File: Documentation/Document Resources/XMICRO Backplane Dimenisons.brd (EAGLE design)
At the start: 203.2 x 70.6 mm, 5 parts

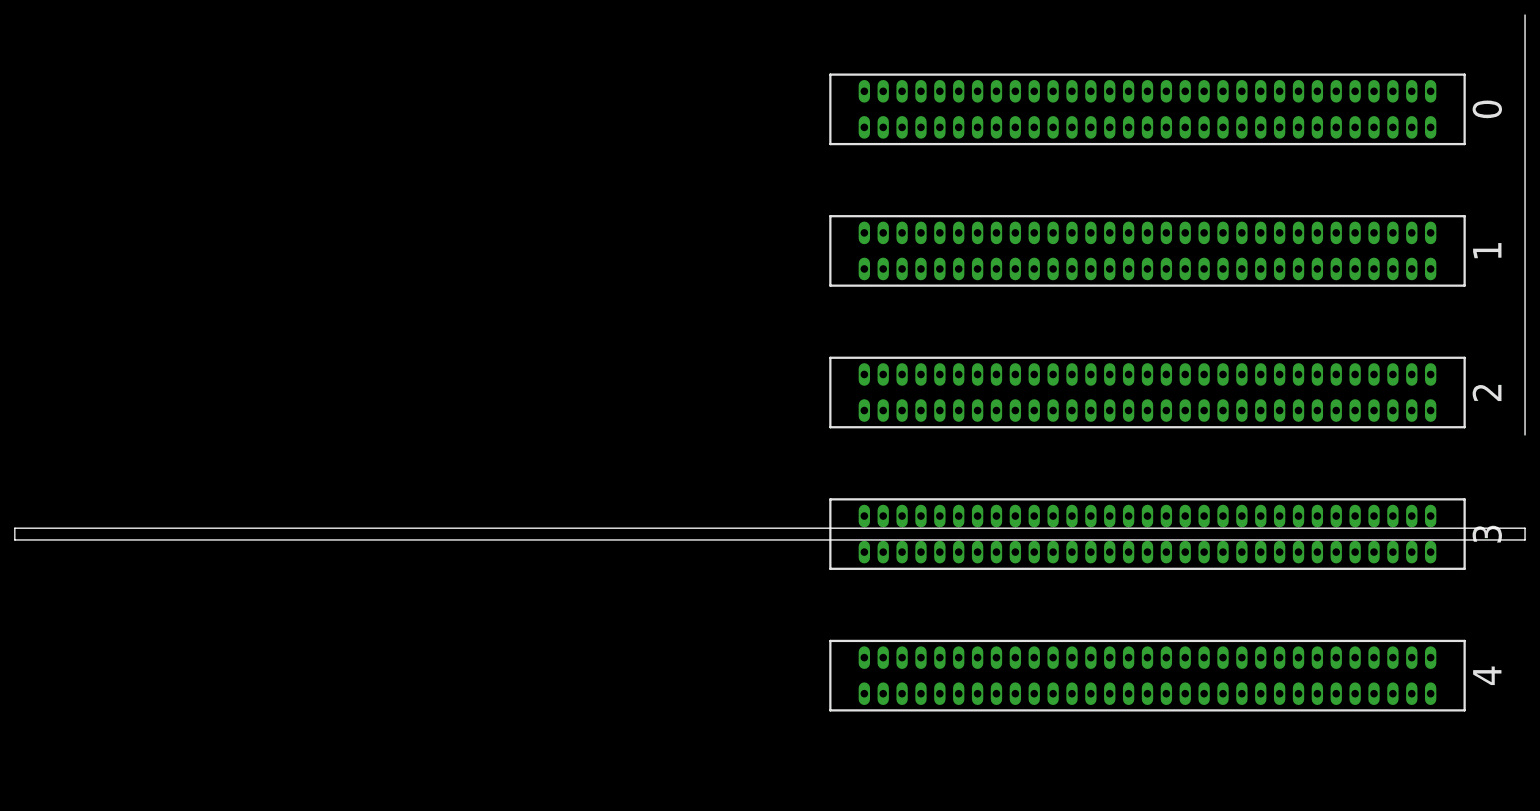
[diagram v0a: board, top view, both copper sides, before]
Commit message: Updating bus specification
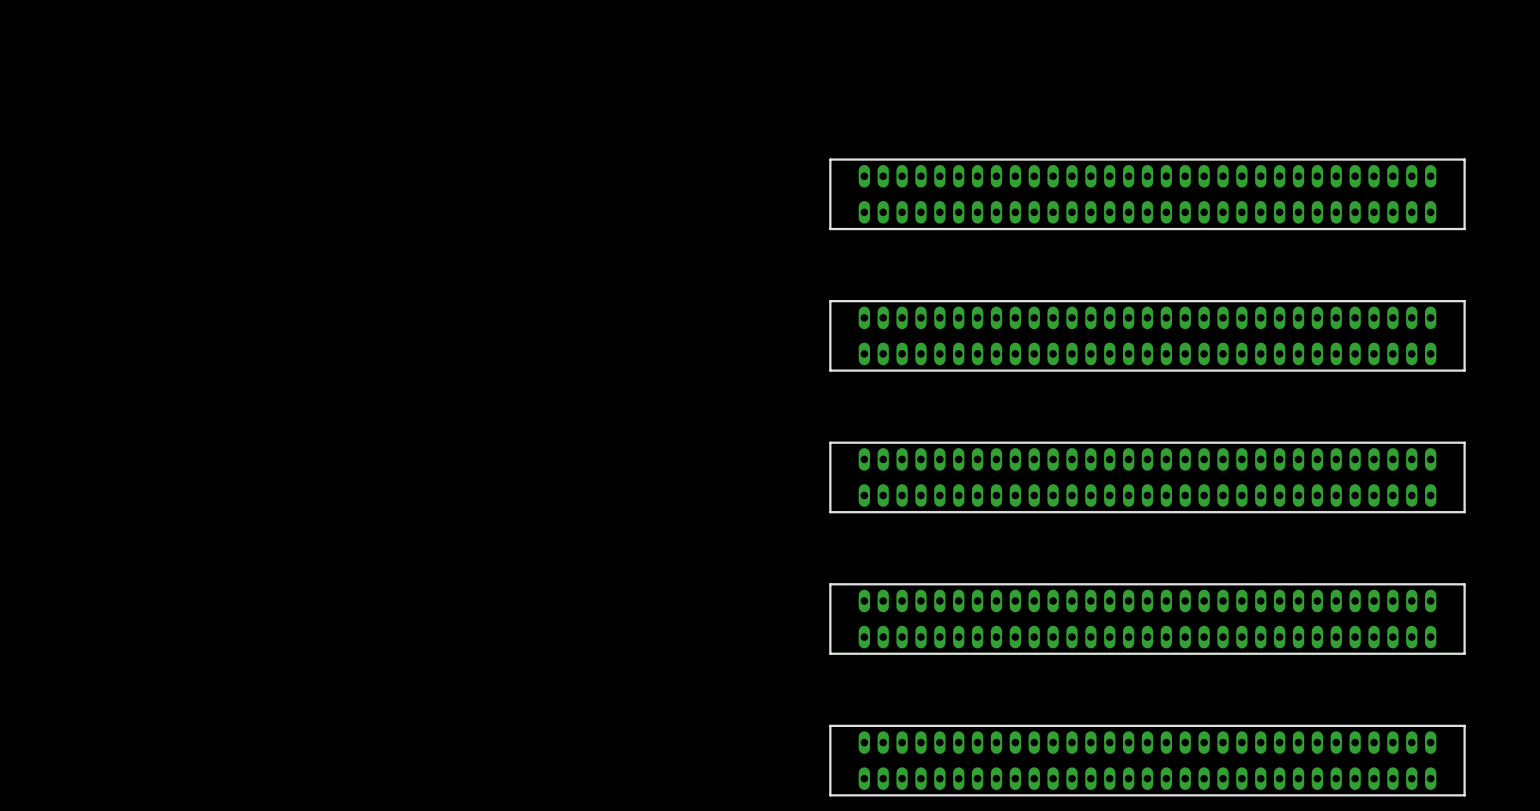
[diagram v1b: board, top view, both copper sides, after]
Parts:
- moved 2 11.4 mm to (152.4, 47.0)
- moved 4 11.4 mm to (152.4, 8.89)
- moved 3 11.4 mm to (152.4, 27.9)
- moved 0 11.4 mm to (152.4, 85.1)
- moved 1 11.4 mm to (152.4, 66.0)
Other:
- board outline removed
- board text added: "CARD MAXIMUM DIMENSIONS"
- board text added: "CARD PCB"
- board text added: "NOTES: 1. All dimensions are in inches"
- board text removed: "CARD DIMENSIONS"
- board text removed: "Notes: 1. All dimensions are in inches 2. Pin 1 must be indicated on at least one slot 3. Each slot number must be indicated on the PCB 4. Maximum component height under cards may not exceed the edge connectors 5. All backplane slots must be capable of receiving full-dimension cards"
